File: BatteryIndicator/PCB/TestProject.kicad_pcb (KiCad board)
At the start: 2 copper layers, 48.3 x 30.5 mm, 6 parts, among them J1_XT60 Conn_01x02_Male, J2_Buck1 Conn_01x03_Female, J3_MCU_Left1 Conn_01x07_Female, J3_MCU_Right1 Conn_01x07_Female, J4_LED1 Conn_01x03_Male, J5_Button1 Conn_01x02_Male

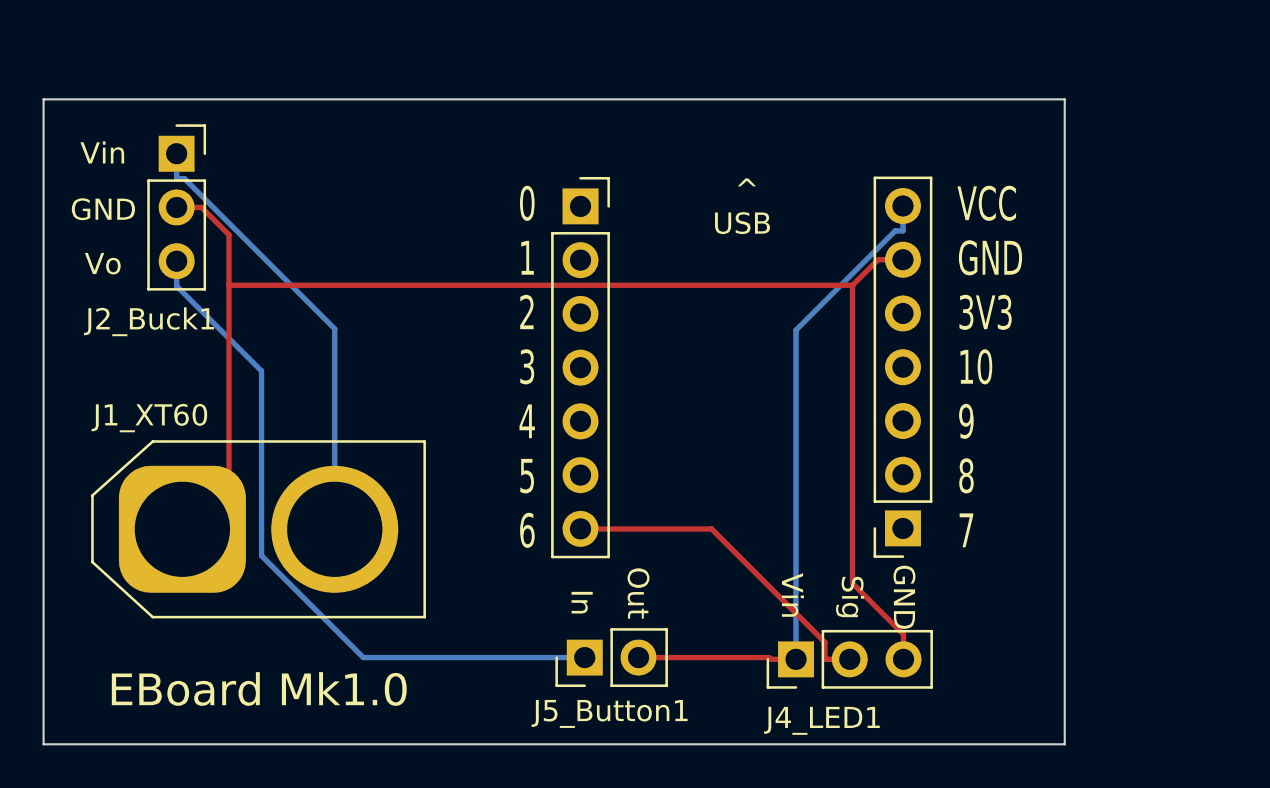
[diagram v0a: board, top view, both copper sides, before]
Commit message: Added UART pins to PCB
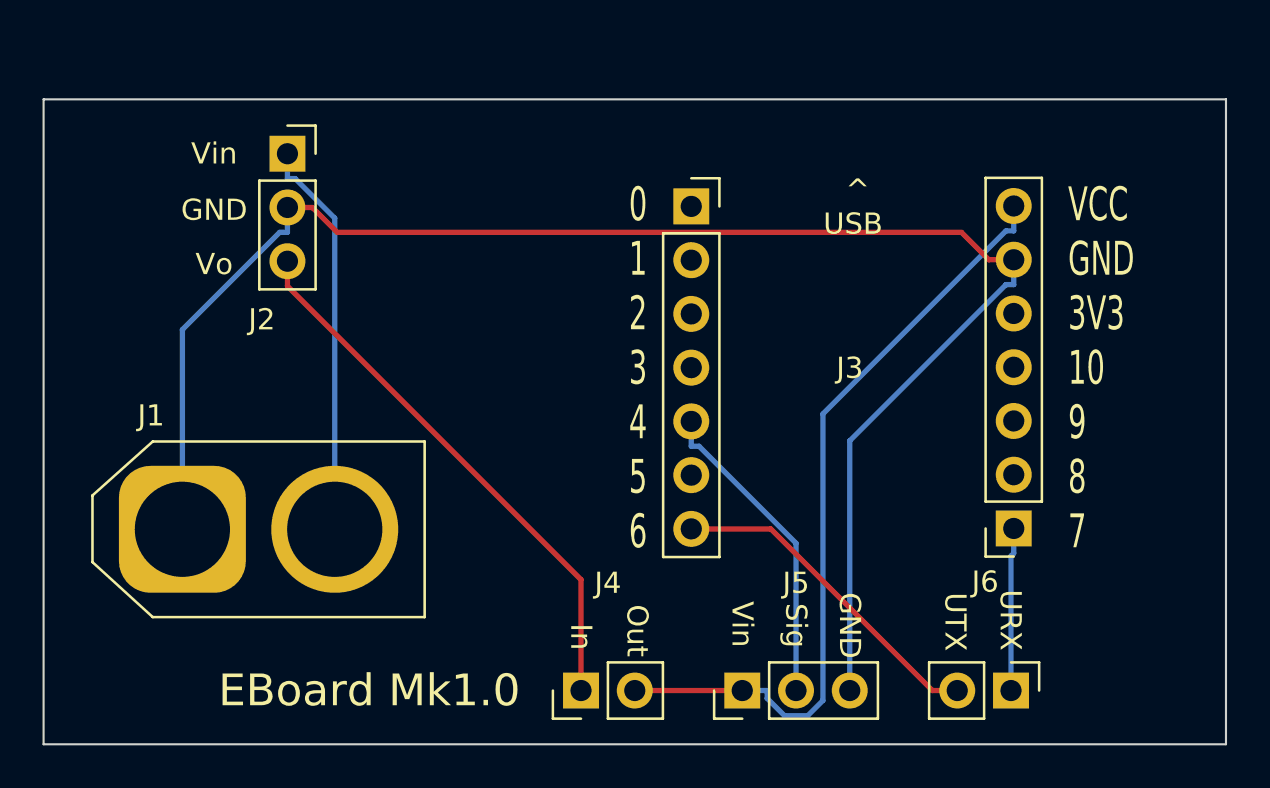
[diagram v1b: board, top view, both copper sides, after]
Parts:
- added J6: Conn_01x02_Male, Connector_PinHeader_2.54mm:PinHeader_1x02_P2.54mm_Vertical, F.Cu at (58.4, 40.6)
- moved J3_1 5.23 mm to (58.5, 33.0)
- moved J2 5.23 mm to (24.2, 15.3)
- moved J3 5.23 mm to (43.3, 17.8)
- moved J5 2.94 mm to (45.7, 40.6)
- moved J4 1.57 mm to (38.1, 40.6)
- renumbered J1_XT60 to J1, J2_Buck1 to J2, J3_MCU_Left1 to J3, J3_MCU_Right1 to J3_1, J5_Button1 to J4, J4_LED1 to J5
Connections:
- J3 pad 5: unconnected-(J3_MCU_Left1-Pad5) -> SIG_LED
- J3 pad 7: SIG_LED -> UART TX
- J3_1 pad 1: unconnected-(J3_MCU_Right1-Pad1) -> UART RX
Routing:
- net UART TX: track 0.00 -> 15.7 mm
- net GND: track 68.9 -> 76.6 mm
- net UART RX: track 0.00 -> 7.71 mm
- net V5: track 32.9 -> 26.0 mm
- net ButtonOut: track 31.2 -> 37.2 mm
- net Vin: track 21.1 -> 18.9 mm
- net SIG_LED: track 15.8 -> 15.0 mm
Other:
- board size 48.3 x 30.5 mm -> 55.9 x 30.5 mm
- board text added: "J1 - Battery In J2 - Buck converter J3 - Xiao RP2040 µP J4 - LED J5 - Button J6 - UART"
- board text added: "J3"
- board text added: "URX"
- board text added: "UTX"

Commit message: Re-added mounting holes
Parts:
- added REF**: MountingHole_3.2mm_M3, MountingHole:MountingHole_3.2mm_M3, F.Cu at (66.0, 40.6)
- added REF**: MountingHole_3.2mm_M3, MountingHole:MountingHole_3.2mm_M3, F.Cu at (15.2, 40.6)
- added REF**: MountingHole_3.2mm_M3, MountingHole:MountingHole_3.2mm_M3, F.Cu at (15.2, 15.2)
- added REF**: MountingHole_3.2mm_M3, MountingHole:MountingHole_3.2mm_M3, F.Cu at (66.0, 15.2)
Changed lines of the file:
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@@
   (net 15 "SIG_LED")
   (net 16 "ButtonOut")
+  (footprint "MountingHole:MountingHole_3.2mm_M3" (layer "F.Cu")
+    (at 66.04 40.64)
+    (descr "Mounting Hole 3.2mm, no annular, M3")
+    (tags "mounting hole 3.2mm no annular m3")
+    (attr exclude_from_pos_files exclude_from_bom)
+    (fp_text reference "REF**" (at 0 -4.2) (layer "F.SilkS")
+      (effects (font (size 1 1) (thickness 0.15)))
+    )
+    (fp_text value "MountingHole_3.2mm_M3" (at 0 4.2) (layer "F.Fab")
+      (effects (font (size 1 1) (thickness 0.15)))
+    )
+    (fp_text user "${REFERENCE}" (at 0 0) (layer "F.Fab")
+      (effects (font (size 1 1) (thickness 0.15)))
+    )
+    (fp_circle (center 0 0) (end 3.2 0) (layer "Cmts.User") (width 0.15) (fill none))
+    (fp_circle (center 0 0) (end 3.45 0) (layer "F.CrtYd") (width 0.05) (fill none))
+    (pad "" np_thru_hole circle (at 0 0) (size 3.2 3.2) (drill 3.2) (layers *.Cu *.Mask))
+  )
+  (footprint "MountingHole:MountingHole_3.2mm_M3" (layer "F.Cu")
+    (at 15.24 40.64)
+    (descr "Mounting Hole 3.2mm, no annular, M3")
+    (tags "mounting hole 3.2mm no annular m3")
+    (attr exclude_from_pos_files exclude_from_bom)
+    (fp_text reference "REF**" (at 0 -4.2) (layer "F.SilkS")
+      (effects (font (size 1 1) (thickness 0.15)))
+    )
+    (fp_text value "MountingHole_3.2mm_M3" (at 0 4.2) (layer "F.Fab")
+      (effects (font (size 1 1) (thickness 0.15)))
+    )
+    (fp_text user "${REFERENCE}" (at 0 0) (layer "F.Fab")
+      (effects (font (size 1 1) (thickness 0.15)))
+    )
+    (fp_circle (center 0 0) (end 3.2 0) (layer "Cmts.User") (width 0.15) (fill none))
+    (fp_circle (center 0 0) (end 3.45 0) (layer "F.CrtYd") (width 0.05) (fill none))
+    (pad "" np_thru_hole circle (at 0 0) (size 3.2 3.2) (drill 3.2) (layers *.Cu *.Mask))
+  )
   (footprint "Connector_PinHeader_2.54mm:PinHeader_1x02_P2.54mm_Vertical" (layer "F.Cu")
     (at 58.42 40.64 -90)
@@
     )
   )
+  (footprint "MountingHole:MountingHole_3.2mm_M3" (layer "F.Cu")
+    (at 15.24 15.24)
+    (descr "Mounting Hole 3.2mm, no annular, M3")
+    (tags "mounting hole 3.2mm no annular m3")
+    (attr exclude_from_pos_files exclude_from_bom)
+    (fp_text reference "REF**" (at 0 -4.2) (layer "F.SilkS")
+      (effects (font (size 1 1) (thickness 0.15)))
+    )
+    (fp_text value "MountingHole_3.2mm_M3" (at 0 4.2) (layer "F.Fab")
+      (effects (font (size 1 1) (thickness 0.15)))
+    )
+    (fp_text user "${REFERENCE}" (at 0 0) (layer "F.Fab")
+      (effects (font (size 1 1) (thickness 0.15)))
+    )
+    (fp_circle (center 0 0) (end 3.2 0) (layer "Cmts.User") (width 0.15) (fill none))
+    (fp_circle (center 0 0) (end 3.45 0) (layer "F.CrtYd") (width 0.05) (fill none))
+    (pad "" np_thru_hole circle (at 0 0) (size 3.2 3.2) (drill 3.2) (layers *.Cu *.Mask))
+  )
   (footprint "Connector_PinSocket_2.54mm:PinSocket_1x07_P2.54mm_Vertical" (layer "F.Cu")
     (at 58.5497 32.98 180)
@@
     )
   )
+  (footprint "MountingHole:MountingHole_3.2mm_M3" (layer "F.Cu")
+    (at 66.04 15.24)
+    (descr "Mounting Hole 3.2mm, no annular, M3")
+    (tags "mounting hole 3.2mm no annular m3")
+    (attr exclude_from_pos_files exclude_from_bom)
+    (fp_text reference "REF**" (at 0 -4.2) (layer "F.SilkS")
+      (effects (font (size 1 1) (thickness 0.15)))
+    )
+    (fp_text value "MountingHole_3.2mm_M3" (at 0 4.2) (layer "F.Fab")
+      (effects (font (size 1 1) (thickness 0.15)))
+    )
+    (fp_text user "${REFERENCE}" (at 0 0) (layer "F.Fab")
+      (effects (font (size 1 1) (thickness 0.15)))
+    )
+    (fp_circle (center 0 0) (end 3.2 0) (layer "Cmts.User") (width 0.15) (fill none))
+    (fp_circle (center 0 0) (end 3.45 0) (layer "F.CrtYd") (width 0.05) (fill none))
+    (pad "" np_thru_hole circle (at 0 0) (size 3.2 3.2) (drill 3.2) (layers *.Cu *.Mask))
+  )
   (footprint "Connector_PinSocket_2.54mm:PinSocket_1x03_P2.54mm_Vertical" (layer "F.Cu")
